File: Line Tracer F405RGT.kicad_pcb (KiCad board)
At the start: 2 copper layers, 100 x 100 mm, 121 parts, among them J1 USB_C_Receptacle_USB2.0, J10 Conn_01x12, J2 Conn_01x04, J3 Conn_01x06, J4 Conn_01x02, J5 Conn_01x06, J6 Conn_01x12, J7 Conn_01x04, J9 Conn_01x02, Q1 AO3401A, Q2 AO3400A, Q3 AO3400A, SW1 SW_SPDT, SW2 RESET, SW3 BUTTON, U1 STM32F405RGTx, U10 ITR8307-S17-TR8, U11 AP2112K-3.3, U12 ITR8307-S17-TR8, U13 TPS5430DDA, U14 ITR8307-S17-TR8, U15 DRV8833PW, U16 DRV8833PW, U2 BMI160, U3 ITR8307-S17-TR8, U4 ITR8307-S17-TR8, U5 ITR8307-S17-TR8, U6 ITR8307-S17-TR8, U7 ITR8307-S17-TR8, U8 ITR8307-S17-TR8, U9 ITR8307-S17-TR8, Y1 16MHz

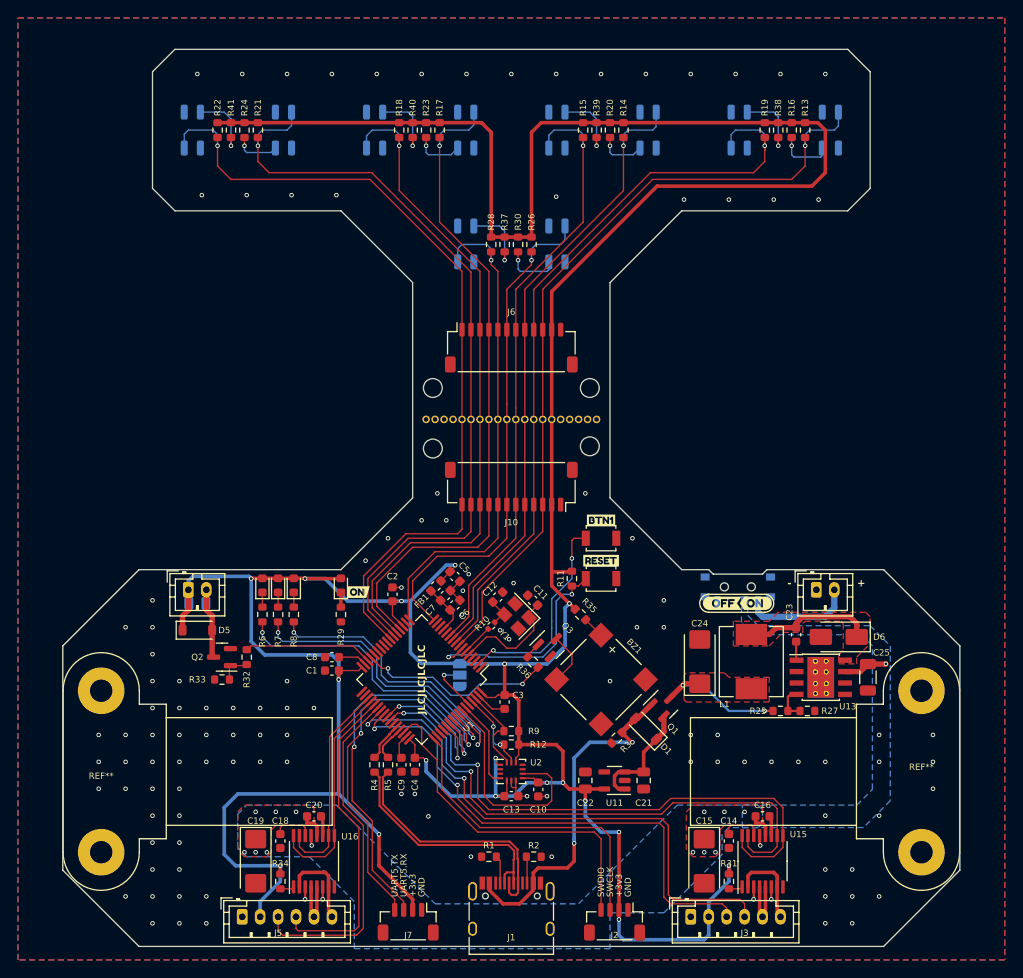
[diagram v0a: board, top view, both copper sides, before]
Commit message: improved sensor design
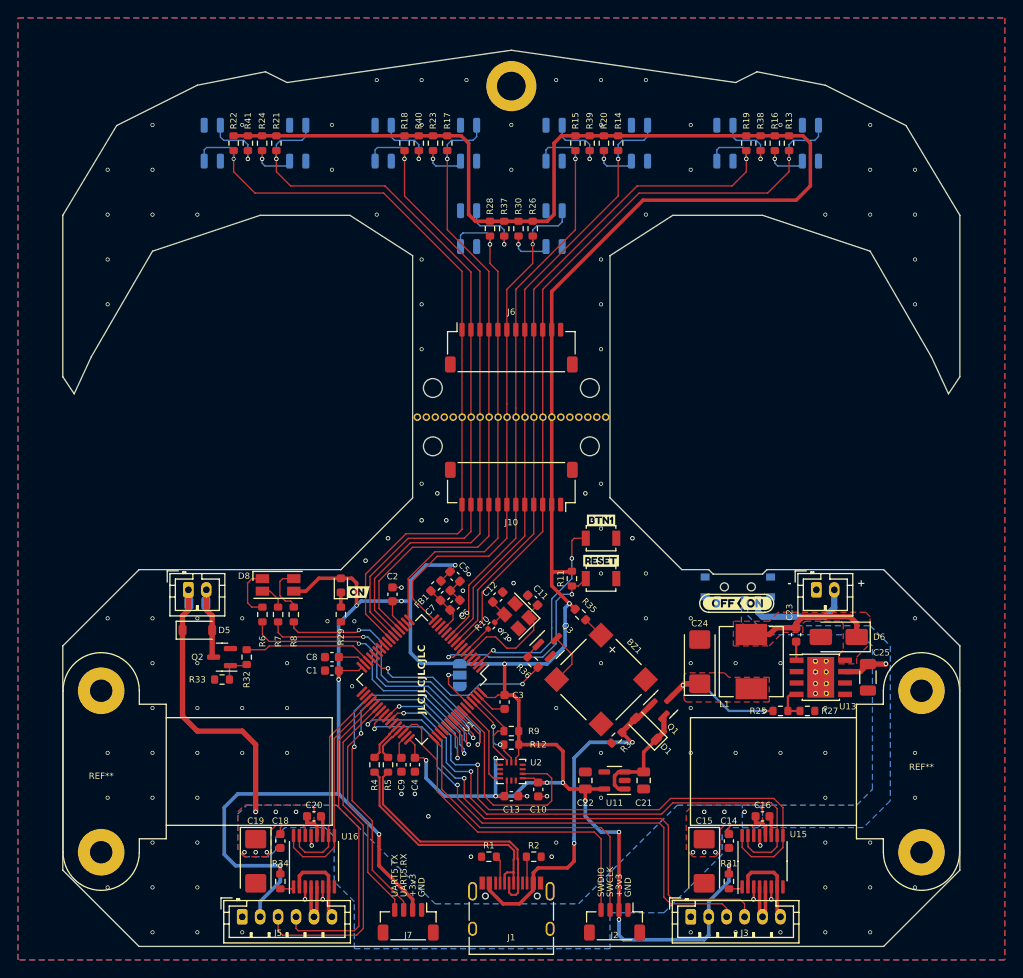
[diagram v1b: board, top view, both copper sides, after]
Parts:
- removed D2: green, LED_SMD:LED_0603_1608Metric
- removed D3: yellow, LED_SMD:LED_0603_1608Metric
- removed D4: blue, LED_SMD:LED_0603_1608Metric
- removed the REF** at (136.6, 86.3)
- added D8: LED_RGAB, LED_SMD:LED_RGB_1210, F.Cu at (120.0, 104.8)
- added REF**: PinHeader_1x22_P1.00mm_Vertical, Connector_PinHeader_1.00mm:PinHeader_1x22_P1.00mm_Vertical, F.Cu at (135.6, 86.1)
- added REF**: MountingHole_3.2mm_M3_DIN965_Pad, MountingHole:MountingHole_3.2mm_M3_DIN965_Pad, F.Cu at (146.1, 49.2)
- moved U3 2.66 mm to (179.4, 55.6)
- moved U10 2.66 mm to (112.7, 55.6)
- moved R19 2.52 mm to (172.2, 55.6)
- moved R21 2.52 mm to (119.9, 55.6)
- moved R24 2.45 mm to (118.3, 55.6)
- moved R38 2.45 mm to (173.8, 55.6)
- moved R16 2.38 mm to (175.4, 55.6)
- moved R41 2.38 mm to (116.7, 55.6)
- moved R13 2.31 mm to (177.0, 55.6)
- moved R22 2.31 mm to (115.1, 55.6)
- moved U9 2.16 mm to (122.2, 55.6)
- moved U7 2.16 mm to (169.9, 55.6)
- moved R28 1.77 mm to (143.7, 65.1)
- moved R26 1.77 mm to (148.4, 65.1)
- moved R37 1.76 mm to (145.3, 65.1)
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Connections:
- C17 pad 1: +3V3 -> V_BATT
- D5 pad 1: +3V3 -> V_BATT
- J4 pad 1: +3V3 -> V_BATT
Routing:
- net +3V3: track 436.8 -> 395.9 mm, vias 18 -> 17
- net V_BATT: track 11.0 -> 42.3 mm
- net /MCU/D2: track 84.6 -> 80.1 mm
- net Net-(D8-RK): track 1.64 -> 5.90 mm
- net /MCU/D8: track 92.3 -> 88.1 mm
- net Net-(D8-BK): track 1.64 -> 5.54 mm
- net /MCU/D7: track 88.6 -> 85.1 mm
- net /MCU/D1: track 88.5 -> 85.3 mm
- net GND: track 20.5 -> 17.4 mm, vias 124 -> 132
- net /MCU/D4: track 68.6 -> 65.6 mm
- net /MCU/D3: track 70.6 -> 67.6 mm
- net /MCU/D6: track 75.7 -> 72.8 mm
- net /MCU/D5: track 74.5 -> 72.1 mm
- net /MCU/MD3: track 56.9 -> 59.2 mm
- net Net-(U12-A): track 6.41 -> 4.92 mm
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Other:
- board size 100 x 100 mm -> 100 x 99.9 mm
